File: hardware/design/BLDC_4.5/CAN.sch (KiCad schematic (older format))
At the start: 4 parts

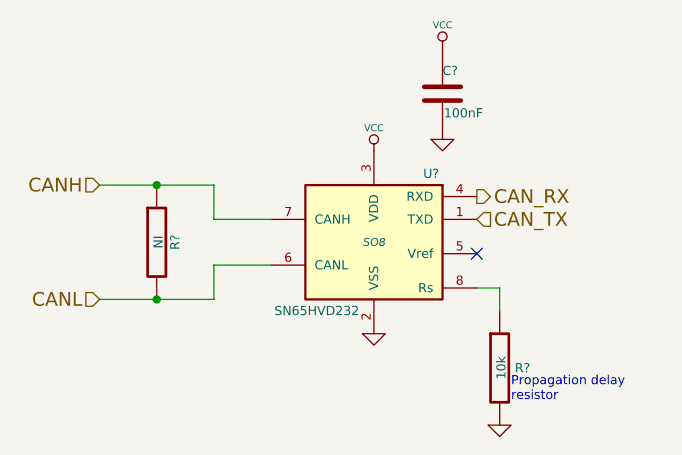
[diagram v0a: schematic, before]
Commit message: Schematic changes: Cleaner top level, added CAN connector, moved LEDs to top level, added 22 Ohm resistors for the USB lines. Fully annotated schematic, ready for layout.
Signed-off-by: Marcos Chaparro <marcos@mrkindustries.com.ar>
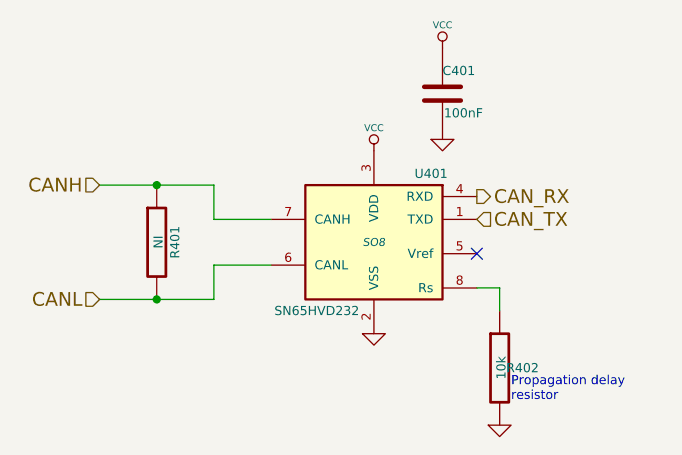
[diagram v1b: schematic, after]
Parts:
- gave numbers to parts that had none: 4
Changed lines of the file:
@@
 LIBS:valves
 LIBS:mrk-industries
+LIBS:crf_1
 LIBS:BLDC_4-cache
 EELAYER 24 0
@@
 $Descr A4 11693 8268
 encoding utf-8
-Sheet 6 6
-Title ""
-Date ""
+Sheet 4 7
+Title "CAN BUS transceiver"
+Date "25 Aug 2014"
 Rev ""
-Comp ""
+Comp "Mrk Industries"
 Comment1 ""
 Comment2 ""
@@
 $EndDescr
 $Comp
-L MCP2551-I/SN U?
+L MCP2551-I/SN U401
 U 1 1 53F59F90
 P 5850 4050
-F 0 "U?" H 5600 4350 40  0000 C CNN
+F 0 "U401" H 5600 4350 40  0000 C CNN
 F 1 "SN65HVD232" H 6100 3750 40  0000 C CNN
 F 2 "SO8" H 5850 4050 35  0000 C CIN
@@
 $EndComp
 $Comp
-L GND #PWR?
+L GND #PWR402
 U 1 1 53F59F97
 P 5850 4450
-F 0 "#PWR?" H 5850 4450 30  0001 C CNN
+F 0 "#PWR402" H 5850 4450 30  0001 C CNN
 F 1 "GND" H 5850 4380 30  0001 C CNN
 F 2 "" H 5850 4450 60  0000 C CNN
@@
 $EndComp
 $Comp
-L VCC #PWR?
+L VCC #PWR401
 U 1 1 53F59F9D
 P 5850 3650
-F 0 "#PWR?" H 5850 3750 30  0001 C CNN
+F 0 "#PWR401" H 5850 3750 30  0001 C CNN
 F 1 "VCC" H 5850 3750 30  0000 C CNN
 F 2 "" H 5850 3650 60  0001 C CNN
@@
 $EndComp
 $Comp
-L C C?
+L C C401
 U 1 1 53F59FA3
 P 6150 3400
-F 0 "C?" H 6150 3500 40  0000 L CNN
+F 0 "C401" H 6150 3500 40  0000 L CNN
 F 1 "100nF" H 6156 3315 40  0000 L CNN
 F 2 "" H 6188 3250 30  0000 C CNN
@@
 $EndComp
 $Comp
-L VCC #PWR?
+L VCC #PWR403
 U 1 1 53F59FAA
 P 6150 3200
-F 0 "#PWR?" H 6150 3300 30  0001 C CNN
+F 0 "#PWR403" H 6150 3300 30  0001 C CNN
 F 1 "VCC" H 6150 3300 30  0000 C CNN
 F 2 "" H 6150 3200 60  0001 C CNN
@@
 $EndComp
 $Comp
-L GND #PWR?
+L GND #PWR404
 U 1 1 53F59FB0
 P 6150 3600
-F 0 "#PWR?" H 6150 3600 30  0001 C CNN
+F 0 "#PWR404" H 6150 3600 30  0001 C CNN
 F 1 "GND" H 6150 3530 30  0001 C CNN
 F 2 "" H 6150 3600 60  0000 C CNN
@@
 CAN_TX
 $Comp
-L R R?
+L R R401
 U 1 1 540030A8
 P 4900 4050
-F 0 "R?" V 4980 4050 40  0000 C CNN
+F 0 "R401" V 4980 4050 40  0000 C CNN
 F 1 "NI" V 4907 4051 40  0000 C CNN
 F 2 "" V 4830 4050 30  0000 C CNN
@@
 NoConn ~ 6300 4100
 $Comp
-L R R?
+L R R402
 U 1 1 54003136
 P 6400 4600
-F 0 "R?" H 6500 4600 40  0000 C CNN
+F 0 "R402" H 6500 4600 40  0000 C CNN
 F 1 "10k" V 6407 4601 40  0000 C CNN
 F 2 "" V 6330 4600 30  0000 C CNN
@@
 	6400 4250 6300 4250
 $Comp
-L GND #PWR?
+L GND #PWR405
 U 1 1 5400318B
 P 6400 4850
-F 0 "#PWR?" H 6400 4850 30  0001 C CNN
+F 0 "#PWR405" H 6400 4850 30  0001 C CNN
 F 1 "GND" H 6400 4780 30  0001 C CNN
 F 2 "" H 6400 4850 60  0000 C CNN

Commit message: Layout updated. Added inner power planes, changed USB connector, added CAN transceiver and connector, added 3D models copper pour under the mosfets and references moved to visible places
Signed-off-by: Marcos Chaparro <marcos@mrkindustries.com.ar>
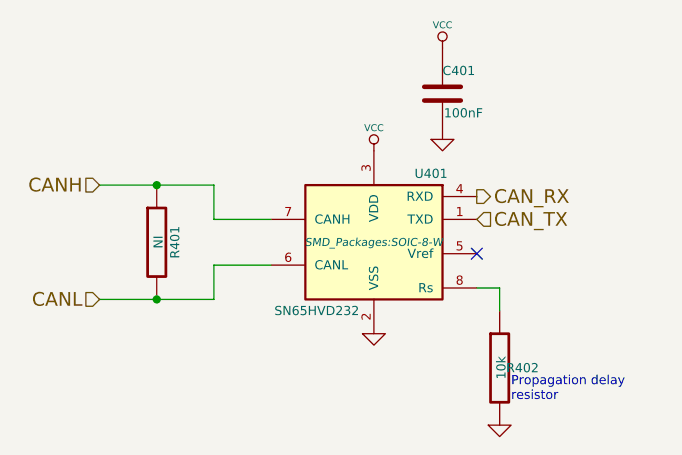
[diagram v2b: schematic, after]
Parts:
- C401: footprint (none) -> SMD_Packages:SMD-0603
- R401, R402: footprint (none) -> SMD_Packages:SMD-0603_r
- U401: footprint SO8 -> SMD_Packages:SOIC-8-W
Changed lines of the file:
@@
 F 0 "U401" H 5600 4350 40  0000 C CNN
 F 1 "SN65HVD232" H 6100 3750 40  0000 C CNN
-F 2 "SO8" H 5850 4050 35  0000 C CIN
+F 2 "SMD_Packages:SOIC-8-W" H 5850 4050 35  0000 C CIN
 F 3 "" H 5850 4050 60  0000 C CNN
 	1    5850 4050
@@
 $EndComp
 $Comp
-L GND #PWR402
+L GND #PWR028
 U 1 1 53F59F97
 P 5850 4450
-F 0 "#PWR402" H 5850 4450 30  0001 C CNN
+F 0 "#PWR028" H 5850 4450 30  0001 C CNN
 F 1 "GND" H 5850 4380 30  0001 C CNN
 F 2 "" H 5850 4450 60  0000 C CNN
@@
 $EndComp
 $Comp
-L VCC #PWR401
+L VCC #PWR029
 U 1 1 53F59F9D
 P 5850 3650
-F 0 "#PWR401" H 5850 3750 30  0001 C CNN
+F 0 "#PWR029" H 5850 3750 30  0001 C CNN
 F 1 "VCC" H 5850 3750 30  0000 C CNN
 F 2 "" H 5850 3650 60  0001 C CNN
@@
 F 0 "C401" H 6150 3500 40  0000 L CNN
 F 1 "100nF" H 6156 3315 40  0000 L CNN
-F 2 "" H 6188 3250 30  0000 C CNN
+F 2 "SMD_Packages:SMD-0603" H 6188 3250 30  0001 C CNN
 F 3 "" H 6150 3400 60  0000 C CNN
 	1    6150 3400
@@
 $EndComp
 $Comp
-L VCC #PWR403
+L VCC #PWR030
 U 1 1 53F59FAA
 P 6150 3200
-F 0 "#PWR403" H 6150 3300 30  0001 C CNN
+F 0 "#PWR030" H 6150 3300 30  0001 C CNN
 F 1 "VCC" H 6150 3300 30  0000 C CNN
 F 2 "" H 6150 3200 60  0001 C CNN
@@
 $EndComp
 $Comp
-L GND #PWR404
+L GND #PWR031
 U 1 1 53F59FB0
 P 6150 3600
-F 0 "#PWR404" H 6150 3600 30  0001 C CNN
+F 0 "#PWR031" H 6150 3600 30  0001 C CNN
 F 1 "GND" H 6150 3530 30  0001 C CNN
 F 2 "" H 6150 3600 60  0000 C CNN
@@
 $Bitmap
 Pos 8850 4800
-Scale 1.000000
+Scale 1,000000
 Data
 89 50 4E 47 0D 0A 1A 0A 00 00 00 0D 49 48 44 52 00 00 01 8D 00 00 01 8C 08 02 00 00 00 A9 99 69
@@
 F 0 "R401" V 4980 4050 40  0000 C CNN
 F 1 "NI" V 4907 4051 40  0000 C CNN
-F 2 "" V 4830 4050 30  0000 C CNN
+F 2 "SMD_Packages:SMD-0603_r" V 4830 4050 30  0001 C CNN
 F 3 "" H 4900 4050 30  0000 C CNN
 	1    4900 4050
@@
 F 0 "R402" H 6500 4600 40  0000 C CNN
 F 1 "10k" V 6407 4601 40  0000 C CNN
-F 2 "" V 6330 4600 30  0000 C CNN
+F 2 "SMD_Packages:SMD-0603_r" V 6330 4600 30  0001 C CNN
 F 3 "" H 6400 4600 30  0000 C CNN
 	1    6400 4600
@@
 	6400 4250 6300 4250
 $Comp
-L GND #PWR405
+L GND #PWR032
 U 1 1 5400318B
 P 6400 4850
-F 0 "#PWR405" H 6400 4850 30  0001 C CNN
+F 0 "#PWR032" H 6400 4850 30  0001 C CNN
 F 1 "GND" H 6400 4780 30  0001 C CNN
 F 2 "" H 6400 4850 60  0000 C CNN
